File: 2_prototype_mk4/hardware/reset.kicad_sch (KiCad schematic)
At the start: 4 parts, among them U3 TXS0101DBV

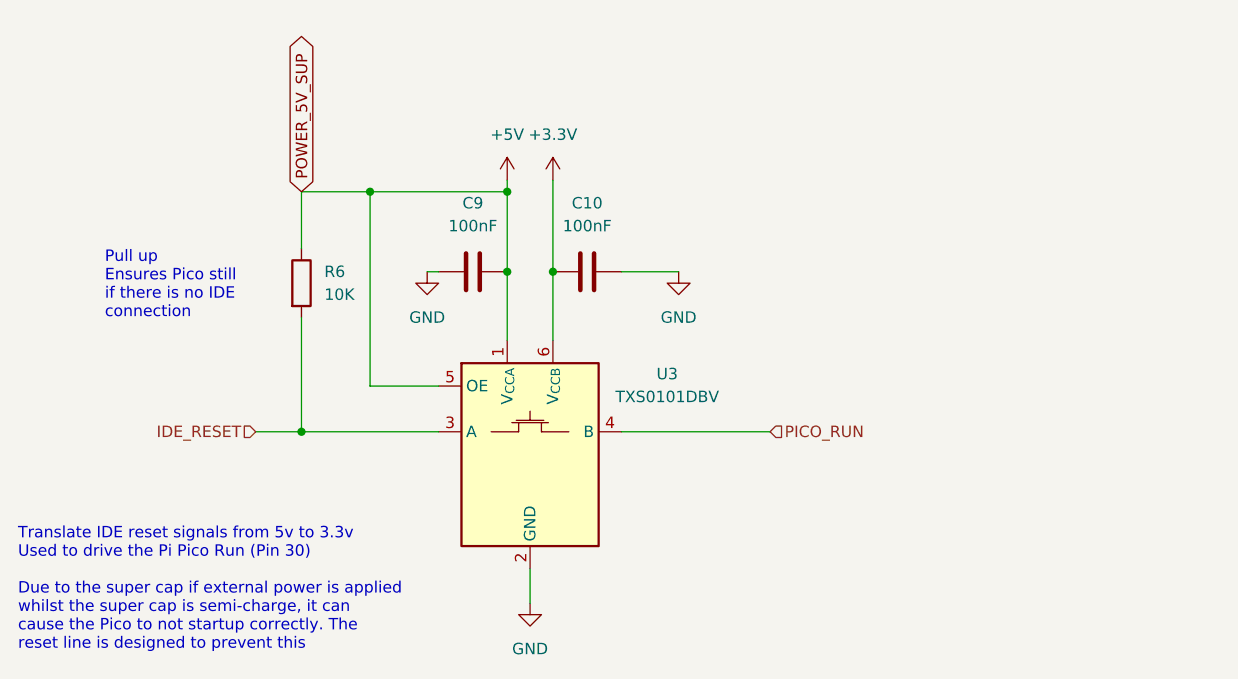
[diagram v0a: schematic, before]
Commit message: MKIV add RGB LED, reset jumper and fixed reset circuit
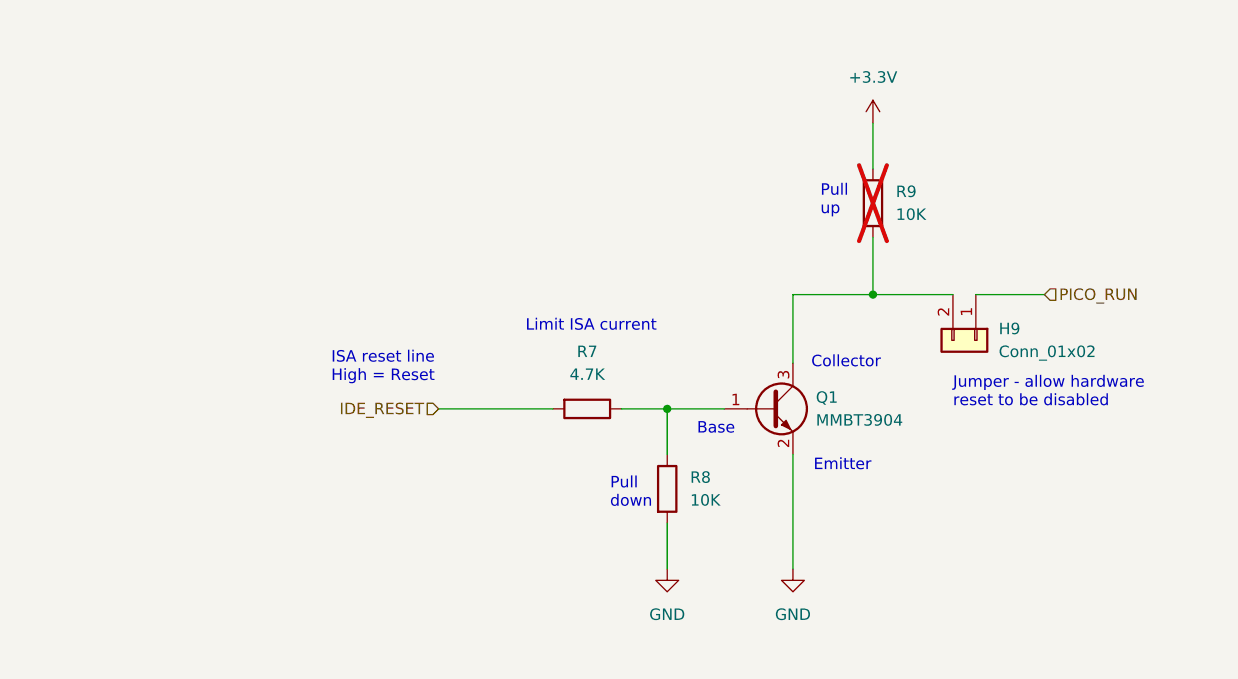
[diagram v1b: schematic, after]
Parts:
- removed C10, C9: 100nF, Capacitor_SMD:C_0402_1005Metric, symbol Device:C
- removed R6: 10K, Resistor_SMD:R_0402_1005Metric, symbol Device:R
- removed U3: TXS0101DBV, Package_TO_SOT_SMD:SOT-23-6, symbol Logic_LevelTranslator:TXS0101DBV
- added H9: Conn_01x02, Connector_PinHeader_2.54mm:PinHeader_1x02_P2.54mm_Vertical, symbol Connector_Generic:Conn_01x02
- added Q1: MMBT3904, Package_TO_SOT_SMD:SOT-23, symbol Transistor_BJT:MMBT3904
- added R7: 4.7K, Resistor_SMD:R_0402_1005Metric, symbol Device:R
- added R8, R9: 10K, Resistor_SMD:R_0402_1005Metric, symbol Device:R
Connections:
- net +3.3V: now also R9.1
- net GND: now also Q1.2 (E), R8.2
- net IDE_RESET: now also R7.2
- net PICO_RUN: now also H9.1 (Pin_1)
- new net: Q1.1 (B), R7.1, R8.1
- new net: H9.2 (Pin_2), Q1.3 (C), R9.2
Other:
- note added: "Base"
- note added: "Collector"
- note added: "Emitter"
- note added: "ISA reset line High = Reset"
- note added: "Jumper - allow hardware reset to be disabled"
- note added: "Limit ISA current"
- note added: "Pull down"
- note added: "Pull up"
- note removed: "Pull up Ensures Pico still if there is no IDE connection"
- note removed: "Translate IDE reset signals from 5v to 3.3v Used to drive the Pi Pico Run (Pin 30) Due to the super cap if external power is applied whilst the super cap is semi-charge, it can cause the Pico to not startup correctly. The reset line is designed to prevent this"
